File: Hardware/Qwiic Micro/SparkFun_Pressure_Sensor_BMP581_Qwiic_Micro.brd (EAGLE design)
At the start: 7.6 x 19.1 mm, 39 parts, among them J1 QWIIC_RIGHT_ANGLE, U1 BMP581

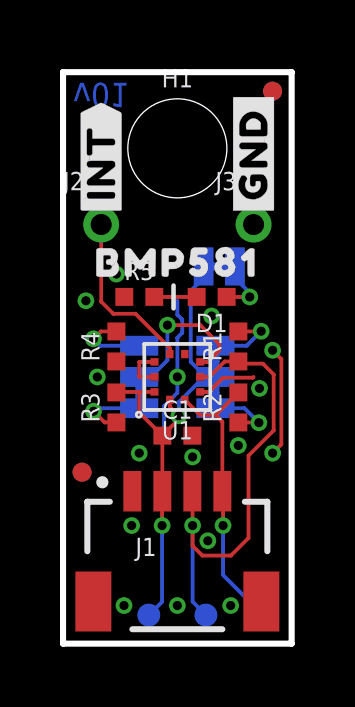
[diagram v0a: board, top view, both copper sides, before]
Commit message: Design review updates
Rename files
Change to v10 (accelerating to reds)
Fix sensor name in schematic
Add note to schematic about max wire diameter in Micro PTH connectors
Update VDD range
Fix acid trap in Micro
Move PWR LED to give space
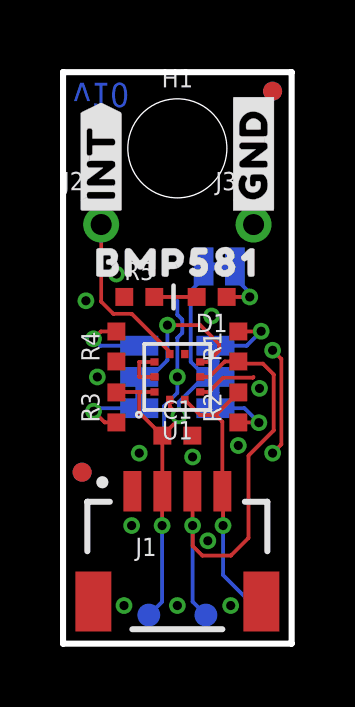
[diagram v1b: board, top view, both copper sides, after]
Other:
- board text added: "v10"
- board text removed: "v01"
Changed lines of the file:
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@@
 <drawing>
 <settings>
-<setting alwaysvectorfont="yes"/>
+<setting alwaysvectorfont="no"/>
 <setting verticaltext="up"/>
 </settings>
-<grid distance="0.05" unitdist="inch" unit="inch" style="lines" multiple="1" display="yes" altdistance="0.001" altunitdist="inch" altunit="inch"/>
+<grid distance="0.05" unitdist="inch" unit="inch" style="lines" multiple="1" display="yes" altdistance="0.005" altunitdist="inch" altunit="inch"/>
 <layers>
 <layer number="1" name="Top" color="4" fill="1" visible="yes" active="yes"/>
@@
 <dimension x1="0" y1="19.05" x2="1.27" y2="19.05" x3="0.635" y3="27.94" textsize="1.778" textratio="15" layer="47" unit="inch"/>
 <text x="-15.24" y="-2.54" size="1.778" layer="47" font="vector" ratio="15">Units: inches</text>
-<text x="1.27" y="18.288" size="0.8128" layer="16" font="vector" ratio="20" rot="SMR180" align="center">v01</text>
+<text x="1.27" y="18.288" size="0.8128" layer="16" font="vector" ratio="20" rot="SMR180" align="center">v10</text>
 <text x="7.62" y="-13.97" size="1.778" layer="51" font="vector">Dryw Wade</text>
 <rectangle x1="2.921" y1="9.0678" x2="3.175" y2="9.2202" layer="41"/>
@@
 <contactref element="U1" pad="7"/>
 <contactref element="J2" pad="1"/>
-<wire x1="3.56" y1="9.8507" x2="2.4172" y2="10.9935" width="0.127" layer="1"/>
-<wire x1="2.4172" y1="10.9935" x2="1.6799625" y2="10.9935" width="0.127" layer="1"/>
+<wire x1="3.56" y1="9.7237" x2="2.2902" y2="10.9935" width="0.127" layer="1"/>
+<wire x1="2.2902" y1="10.9935" x2="1.6799625" y2="10.9935" width="0.127" layer="1"/>
 <wire x1="1.6799625" y1="10.9935" x2="1.27" y2="11.4034625" width="0.127" layer="1"/>
 <wire x1="1.27" y1="11.4034625" x2="1.27" y2="13.97" width="0.127" layer="1"/>
-<wire x1="3.56" y1="9.6525" x2="3.56" y2="9.8507" width="0.127" layer="1"/>
+<wire x1="3.56" y1="9.6525" x2="3.56" y2="9.7237" width="0.127" layer="1"/>
 </signal>
 <signal name="!CSB!">
